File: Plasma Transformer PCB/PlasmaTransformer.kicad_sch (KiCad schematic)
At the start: 74 parts, among them J1 Barrel_Jack_MountingPin, J11 Screw_Terminal_01x01, J12 Screw_Terminal_01x01, J2 Conn_01x02_Pin, J3 Conn_Coaxial, J4 Conn_02x04_Odd_Even, J5 Conn_Coaxial, J6 Conn_01x02_Pin, J7 Conn_01x02_Pin, J8 AudioJack3, M1 Fan, Q1 Q_NMOS_Depletion_GDS, Q2 BUK9832-55A, SW1 SW_SPDT, U1 LM397

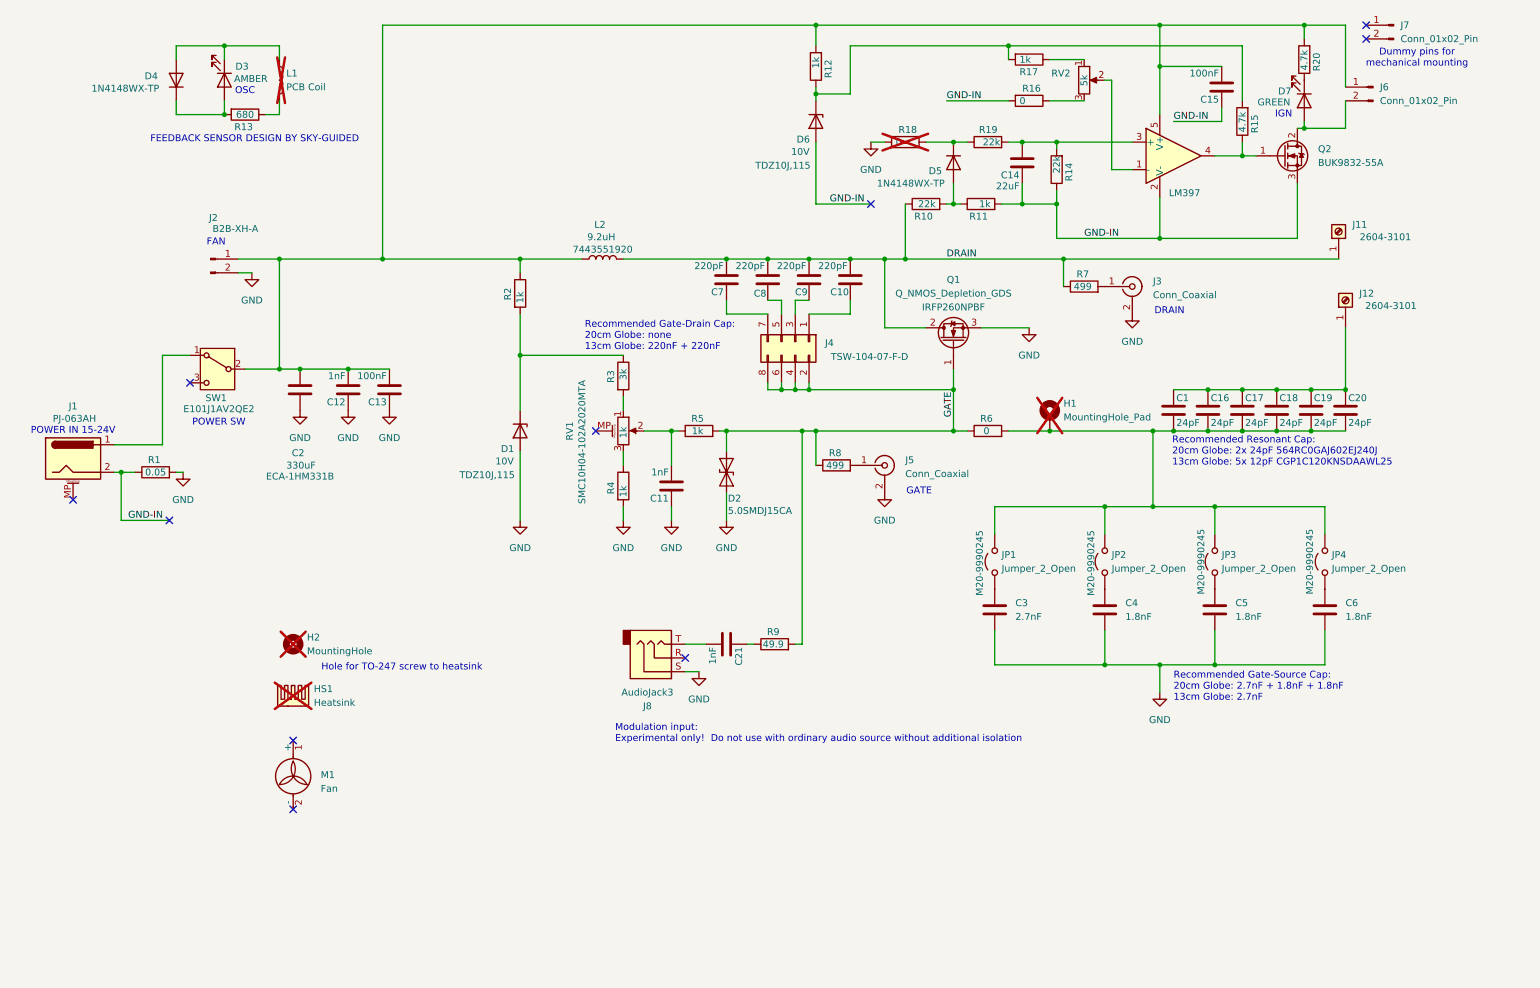
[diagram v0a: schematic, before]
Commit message: Rolling auto igniter Rev 4 into the main folder
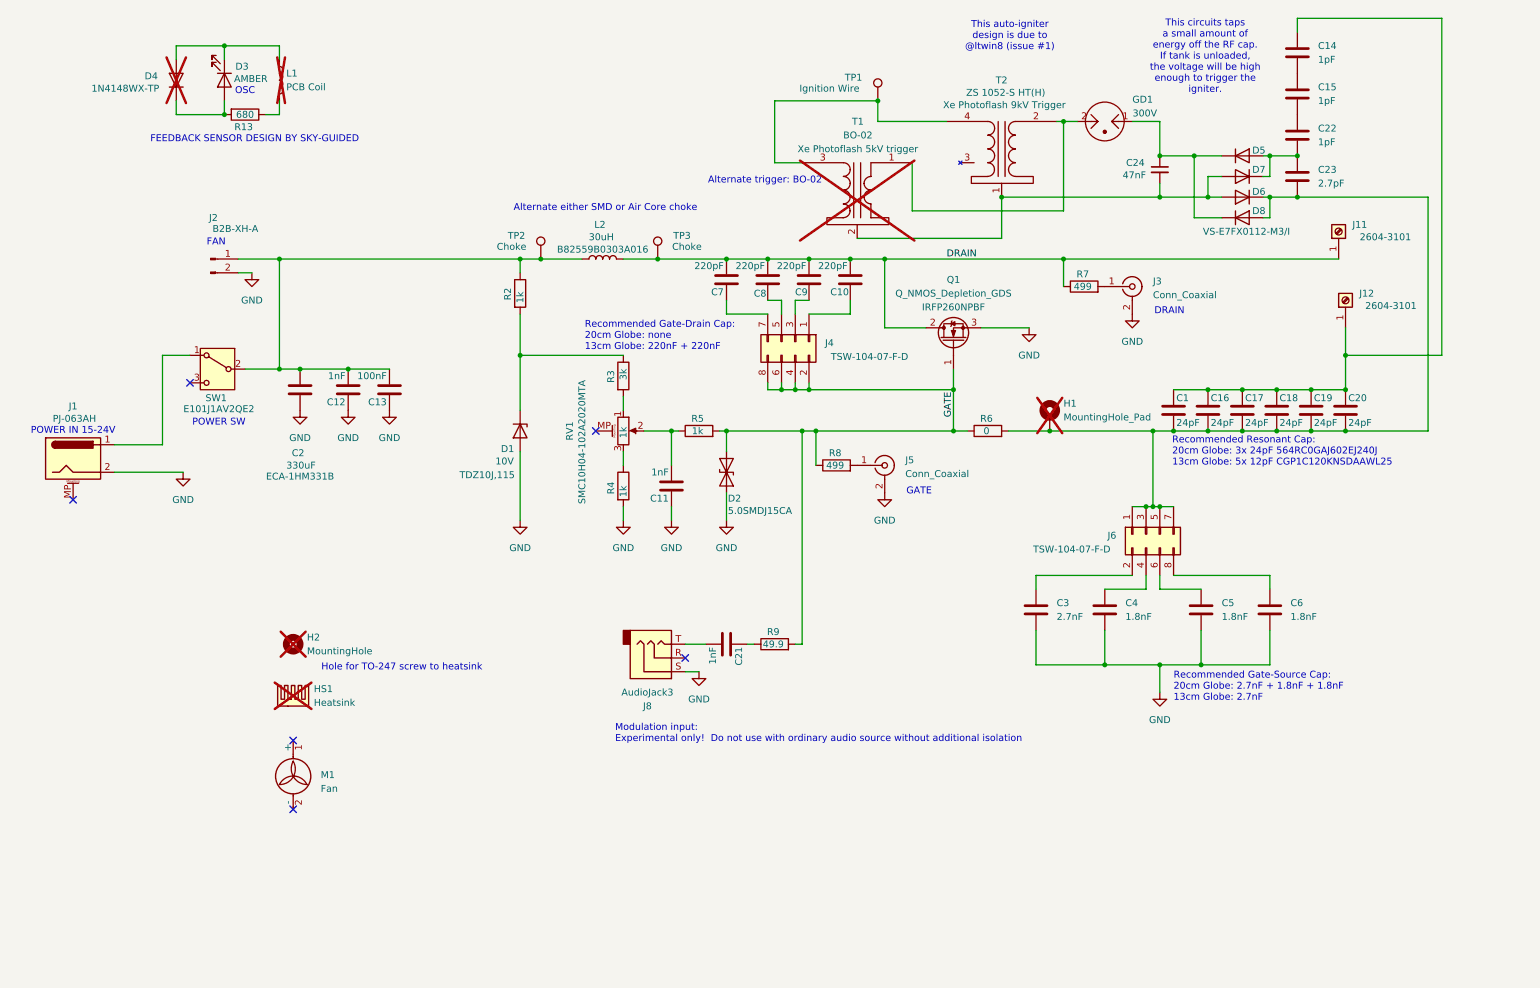
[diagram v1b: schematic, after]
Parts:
- removed D6: 10V, Diode_SMD:D_SOD-323_HandSoldering, symbol Device:D_Zener
- removed D7: GREEN, LED_SMD:LED_1206_3216Metric, symbol Device:LED
- removed J6, J7: Conn_01x02_Pin, Connector_PinHeader_2.54mm:PinHeader_1x02_P2.54mm_Vertical, symbol Connector:Conn_01x02_Pin
- removed JP1, JP2, JP3, JP4: Jumper_2_Open, Connector_PinHeader_2.54mm:PinHeader_1x02_P2.54mm_Vertical, symbol Jumper:Jumper_2_Open
- removed Q2: BUK9832-55A, Package_TO_SOT_SMD:SOT-223-3_TabPin2, symbol Transistor_FET:BUK9832-55A
- removed R1: 0.05, Resistor_SMD:R_2512_6332Metric, symbol Device:R
- removed R10, R14, R19: 22k, Resistor_SMD:R_0805_2012Metric, symbol Device:R
- removed R11, R12, R17: 1k, Resistor_SMD:R_0805_2012Metric, symbol Device:R
- removed R15, R20: 4.7k, Resistor_SMD:R_0805_2012Metric, symbol Device:R
- removed R16, R18: 0, Resistor_SMD:R_0805_2012Metric, symbol Device:R
- removed RV2: 5k, Potentiometer_SMD:Potentiometer_Vishay_TS53YL_Vertical, symbol Device:R_Potentiometer
- removed U1: LM397, Package_TO_SOT_SMD:SOT-23-5, symbol Comparator:LM397
- added C22: 1pF, Capacitor_SMD:C_1210_3225Metric, symbol Device:C
- added C23: 2.7pF, Capacitor_SMD:C_1210_3225Metric, symbol Device:C
- added C24: 47nF, Capacitor_SMD:C_1206_3216Metric, symbol Device:C_Small
- added D6, D7, D8: D, Diode_SMD:D_SMB, symbol Device:D
- added GD1: 300V, Inductor_SMD:L_1812_4532Metric, symbol Device:GDT_2Pin
- added J6: Conn_02x04_Odd_Even, Connector_PinHeader_2.54mm:PinHeader_2x04_P2.54mm_Vertical, symbol Connector_Generic:Conn_02x04_Odd_Even
- added T1: BO-02, ALibrary:BO-02, symbol ALibrary:BO-02
- added T2: ZS 1052-S HT(H), ALibrary:ZS 1052-S HT(H), symbol _Xenon:ZS_1052-S_HT(H)
- added TP1: Ignition Wire, Connector_Wire:SolderWire-0.75sqmm_1x01_D1.25mm_OD2.3mm, symbol Connector:TestPoint
- added TP2, TP3: Choke, Connector_Wire:SolderWire-1sqmm_1x01_D1.4mm_OD2.7mm, symbol Connector:TestPoint
- C14: value 22uF -> 1pF; footprint Capacitor_SMD:C_0805_2012Metric -> Capacitor_SMD:C_1210_3225Metric; MPN GRM21BR61E226ME44L -> 111122K01P00BQTAF9LM; Manufacturer Murata -> Knowles Syfer
- C15: value 100nF -> 1pF; footprint Capacitor_SMD:C_0805_2012Metric -> Capacitor_SMD:C_1210_3225Metric; MPN CL21B104KCFNNNE -> 111122K01P00BQTAF9LM; Manufacturer Samsung -> Knowles Syfer
- D4: now not fitted
- D5: footprint Diode_SMD:D_SOD-323 -> Diode_SMD:D_SMB; MPN 1N4148WX-TP -> VS-E7FX0112-M3/I; Manufacturer MCC -> Vishay
- L2: value 9.2uH -> 30uH; footprint Inductor_SMD:L_APV_APH1770 -> ALibrary:B82559B_TDK; MPN 7443551920 -> B82559B0303A016
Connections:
- net DRAIN: now also TP3.1
- net GND: now also J1.2
- net at C12.2, C13.2, C2.1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: now also TP2.1; no longer C15.2
- net at C6.1: now also J6.8 (Pin_8)
- net at C1.2, C16.2, C17.2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: now also C23.2, D6.1 (K), D8.2 (A), J6.1 (Pin_1), J6.3 (Pin_3), J6.5 (Pin_5), J6.7 (Pin_7)
- net at D5.1 (K): now also C24.1, D8.1 (K), GD1.1
- net at C14.2: now also C15.1
- net at C5.1: now also J6.6 (Pin_6)
- net at C1.1, C16.1, C17.1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: now also C14.1
- net at C4.1: now also J6.4 (Pin_4)
- net at D5.2 (A): now also C22.2, C23.1, D7.1 (K)
- net at C3.1: now also J6.2 (Pin_2)
- removed net GND-IN: C14.1, C15.1, J1.2
- new net: C15.2, C22.1
- new net: GD1.2, T1.1 (Primary), T2.2 (AA)
- new net: C24.2, D6.2 (A), D7.2 (A), T1.2 (AB), T2.1 (AB)
- new net: T1.3 (Secondary), T2.4 (SB), TP1.1
- no-connect marks 10 -> 6
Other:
- note added: "Alternate either SMD or Air Core choke"
- note added: "Alternate trigger: BO-02"
- note added: "Recommended Resonant Cap: 20cm Globe: 3x 24pF 564RC0GAJ602EJ240J 13cm Globe: 5x 12pF CGP1C120KNSDAAWL25"
- note added: "This auto-igniter design is due to @ltwin8 (issue #1)"
- note added: "This circuits taps a small amount of energy off the RF cap. If tank is unloaded, the voltage will be high enough to trigger the igniter."
- note removed: "Dummy pins for mechanical mounting"
- note removed: "IGN"
- note removed: "Recommended Resonant Cap: 20cm Globe: 2x 24pF 564RC0GAJ602EJ240J 13cm Globe: 5x 12pF CGP1C120KNSDAAWL25"
- moved on the sheet: C3, C5, C6

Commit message: Rev 4 publish, silkscreen fixes, adding 3d models and footprint library.
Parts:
- J11, J12: footprint Library:CONN_2604-3101_WAG -> ALibrary:CONN_2604-3101_WAG
- J3, J5: footprint Connector_Coaxial:SMA_Amphenol_901-143_Horizontal -> ALibrary:SMA_Amphenol_901-144_Vertical; MPN RFPC-SMA27-F -> RFPC-SMA28-F
- J8: footprint Connector_Audio:Jack_3.5mm_CUI_SJ-3523-SMT_Horizontal -> ALibrary:Jack_3.5mm_CUI_SJ-3523-SMT_Horizontal
- SW1: footprint Library:CKSW-E101J1AV2QE2 -> ALibrary:CKSW-E101J1AV2QE2
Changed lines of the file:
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@@
 			)
 		)
-		(property "Footprint" "Connector_Coaxial:SMA_Amphenol_901-143_Horizontal"
+		(property "Footprint" "ALibrary:SMA_Amphenol_901-144_Vertical"
 			(at 172.72 97.79 0)
 			(effects
@@
 			)
 		)
-		(property "MPN" "RFPC-SMA27-F"
+		(property "MPN" "RFPC-SMA28-F"
 			(at 172.72 97.79 0)
 			(effects
@@
 			)
 		)
-		(property "Footprint" "Connector_Coaxial:SMA_Amphenol_901-143_Horizontal"
+		(property "Footprint" "ALibrary:SMA_Amphenol_901-144_Vertical"
 			(at 218.44 64.77 0)
 			(effects
@@
 			)
 		)
-		(property "MPN" "RFPC-SMA27-F"
+		(property "MPN" "RFPC-SMA28-F"
 			(at 218.44 64.77 0)
 			(effects
@@
 			)
 		)
-		(property "Footprint" "Connector_Audio:Jack_3.5mm_CUI_SJ-3523-SMT_Horizontal"
+		(property "Footprint" "ALibrary:Jack_3.5mm_CUI_SJ-3523-SMT_Horizontal"
 			(at 130.81 133.35 0)
 			(effects
@@
 			)
 		)
-		(property "Footprint" "Library:CKSW-E101J1AV2QE2"
+		(property "Footprint" "ALibrary:CKSW-E101J1AV2QE2"
 			(at 49.53 80.01 0)
 			(effects
@@
 			)
 		)
-		(property "Footprint" "Library:CONN_2604-3101_WAG"
+		(property "Footprint" "ALibrary:CONN_2604-3101_WAG"
 			(at 256.54 54.61 0)
 			(effects
@@
 			)
 		)
-		(property "Footprint" "Library:CONN_2604-3101_WAG"
+		(property "Footprint" "ALibrary:CONN_2604-3101_WAG"
 			(at 257.81 67.31 0)
 			(effects

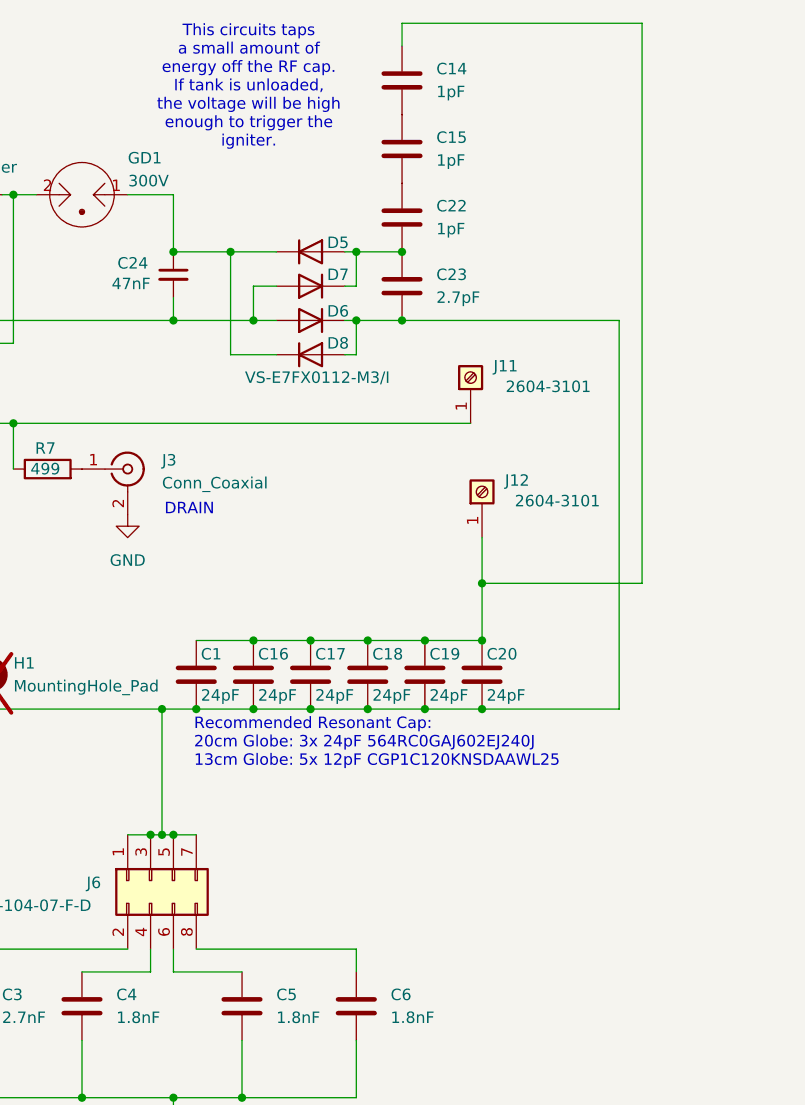
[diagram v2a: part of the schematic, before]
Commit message: convert tank caps to push fit sockets
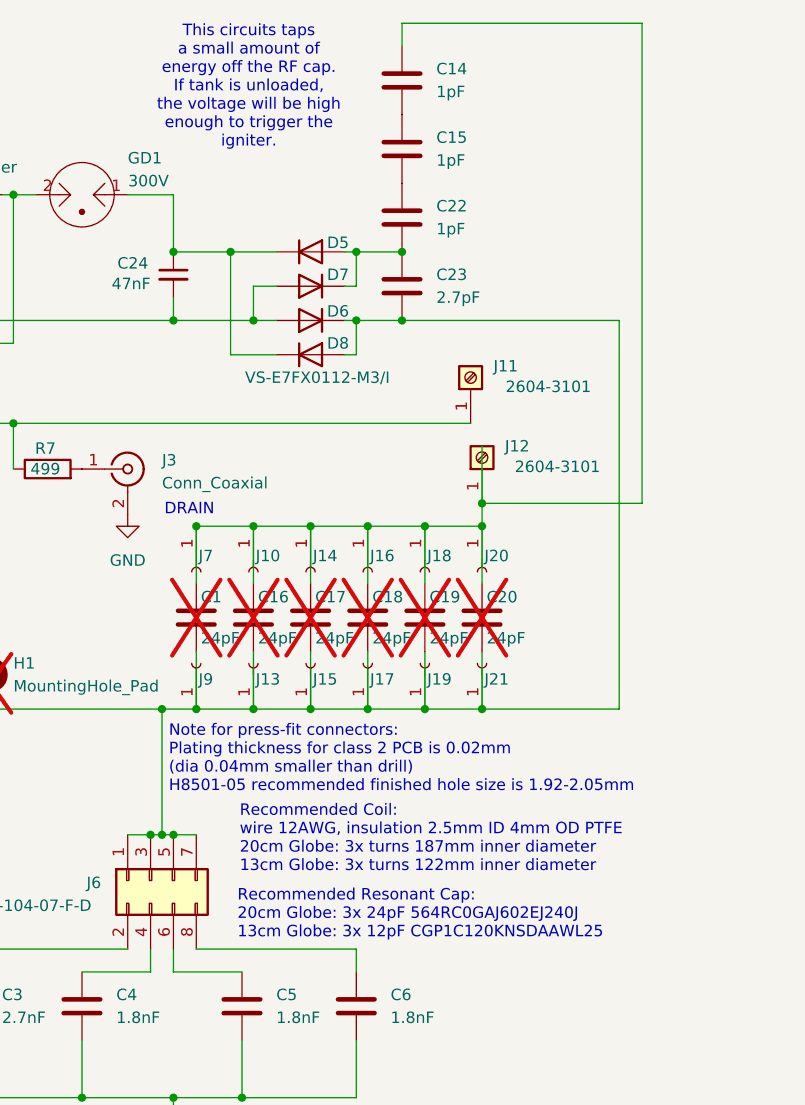
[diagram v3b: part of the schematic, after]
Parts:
- added J10, J13, J14, J15, J16, J17, J18, J19, J20, J21, J7, J9: Conn_01x01_Socket, ALibrary:H8501-05, symbol Connector:Conn_01x01_Socket
- C1, C16, C17, C18, C19, C20: now not fitted
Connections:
- net at C1.2, C16.2, C17.2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: now also J13.1 (Pin_1), J15.1 (Pin_1), J17.1 (Pin_1), J19.1 (Pin_1), J21.1 (Pin_1), J9.1 (Pin_1)
- net at C1.1, C14.1, C16.1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: now also J10.1 (Pin_1), J14.1 (Pin_1), J16.1 (Pin_1), J18.1 (Pin_1), J20.1 (Pin_1), J7.1 (Pin_1)
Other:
- note added: "Note for press-fit connectors: Plating thickness for class 2 PCB is 0.02mm (dia 0.04mm smaller than drill) H8501-05 recommended finished hole size is 1.92-2.05mm"
- note added: "Recommended Coil: wire 12AWG, insulation 2.5mm ID 4mm OD PTFE 20cm Globe: 3x turns 187mm inner diameter 13cm Globe: 3x turns 122mm inner diameter"
- note added: "Recommended Resonant Cap: 20cm Globe: 3x 24pF 564RC0GAJ602EJ240J 13cm Globe: 3x 12pF CGP1C120KNSDAAWL25"
- note removed: "Recommended Resonant Cap: 20cm Globe: 3x 24pF 564RC0GAJ602EJ240J 13cm Globe: 5x 12pF CGP1C120KNSDAAWL25"
- moved on the sheet: J12

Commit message: WIP rev 5 rebase
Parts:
- removed J10, J13, J14, J15, J16, J17, J18, J19, J20, J21, J7, J9: Conn_01x01_Socket, ALibrary:H8501-05, symbol Connector:Conn_01x01_Socket
- added C25, C26: 4.7uF, Capacitor_SMD:C_1210_3225Metric, symbol Device:C
- added C27, C28: 100nF, Capacitor_SMD:C_0805_2012Metric, symbol Device:C
- added C29: 22uF, Capacitor_SMD:C_0805_2012Metric, symbol Device:C
- added L3: 56uH, Inductor_SMD:L_Bourns_SRR1210A, symbol Device:L
- added R1: 100k, Resistor_SMD:R_0805_2012Metric, symbol Device:R
- added R10: 7.15k, Resistor_SMD:R_0805_2012Metric, symbol Device:R
- added U1: LMR51610YDBVR, Package_TO_SOT_SMD:SOT-23-6, symbol Regulator_Switching:LMR14206
- C1, C16, C17, C18, C19, C20: now fitted
- C10, C7, C8, C9, J4: now not fitted
- C2: symbol Device:C -> Device:C_Polarized_US; MPN ECA-1HM331B -> ECA-1JHG331; Voltage (none) -> 63V
- D5, D6, D7, D8: footprint Diode_SMD:D_SMB -> Diode_SMD:D_SMF
- RV1: footprint Library:SMC10H04-102A2020MTA -> ALibrary:SMC10H04-102A2020MTA
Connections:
- net DRAIN: now also C14.1
- net GND: now also C25.2, C26.2, C27.1, C29.1, R10.2, U1.2 (GND)
- net at C1.1, C16.1, C17.1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: no longer C14.1
- net +V: now reaches C12.2, C13.2, C2.1, L2.1, SW1.2 (B), TP2.1
- net +V: now also C25.1, C26.1, C27.2, U1.4 (~{SHDN}), U1.5 (VIN); no longer J2.1 (Pin_1), R2.1
- net REF10V: now reaches D1.1 (K), R2.2, R3.1
- net VIN: now reaches J1.1, SW1.1 (A)
- new net: C28.1, L3.1, U1.6 (SW)
- new net: R1.2, R10.1, U1.3 (FB)
- new net: C28.2, U1.1 (CB)
- new net +12V: C29.2, J2.1 (Pin_1), L3.2, R1.1, R2.1
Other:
- note added: "12V SUPPLY FOR FAN AND GATE CONTROL VREF"
- note added: "AUTO IGNITION CIRCUIT"
- note added: "CHOKE"
- note added: "CONNECTION TO PLASMA COIL"
- note added: "Experimental only! Do not use with ordinary audio source without additional isolation"
- note added: "GATE BIAS CONTROL"
- note added: "GATE FEEDBACK CAP DIVIDER"
- note added: "IGNITION WIRE"
- note added: "MODULATION INPUT"
- note added: "MOSFET"
- note added: "Mount for optional doorknob tank cap"
- note added: "OSCILLATION INDICATOR"
- note added: "OSCILLOSCOPE PROBE - DRAIN"
- note added: "OSCILLOSCOPE PROBE - GATE"
- note added: "PLASMA TRANSFORMER REV 5"
- note added: "POWER IN 12.5-65V"
- note added: "POWER INPUT (12.5-65V)"
- note added: "Recommended Coil 12AWG Wire, PTFE tube insulation 2.5mm ID 4mm OD 20cm Globe: 3 turns, 187mm dia 13cm Globe: 4 turns, 122mm dia"
- note added: "Recommended Gate-Drain Cap: 20cm Globe: none 13cm Globe: none"
- note added: "Recommended Resonant Cap: 20cm Globe: 3x 24pF 564RC0GAJ602EJ240J 13cm Globe: 3x 24pF 564RC0GAJ602EJ240J"
- note added: "TANK CAP"
- note added: "design credit to @ltwin8 (issue #1)"
- note added: "design credit to Sky-Guided"
- note added: "place end in contact with globe"
- note removed: "DRAIN"
- note removed: "FEEDBACK SENSOR DESIGN BY SKY-GUIDED"
- note removed: "GATE"
- note removed: "Modulation input: Experimental only! Do not use with ordinary audio source without additional isolation"
- note removed: "Note for press-fit connectors: Plating thickness for class 2 PCB is 0.02mm (dia 0.04mm smaller than drill) H8501-05 recommended finished hole size is 1.92-2.05mm"
- note removed: "POWER IN 15-24V"
- note removed: "Recommended Coil: wire 12AWG, insulation 2.5mm ID 4mm OD PTFE 20cm Globe: 3x turns 187mm inner diameter 13cm Globe: 3x turns 122mm inner diameter"
- note removed: "Recommended Gate-Drain Cap: 20cm Globe: none 13cm Globe: 220nF + 220nF"
- note removed: "Recommended Resonant Cap: 20cm Globe: 3x 24pF 564RC0GAJ602EJ240J 13cm Globe: 3x 12pF CGP1C120KNSDAAWL25"
- note removed: "This auto-igniter design is due to @ltwin8 (issue #1)"
- moved on the sheet: C11, C12, C13, C14, C15, C21, C22, C23, C24, C3, C4, C5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
